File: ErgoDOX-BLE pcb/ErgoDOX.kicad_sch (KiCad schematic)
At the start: 113 parts, among them J1 Conn_01x04, J2 Conn_01x02_Female, J4 Conn_01x02, J5 Conn_01x02, J6 6PIN, P1 USB_C_Plug_USB2.0, Q1 Q_NPN_BCE, SW0:10 SW0:3, SW0:11 SW0:2, SW0:12 SW0:1, SW0:7 SW0:6, SW0:8 SW0:5, SW0:9 SW0:4, SW1:10 SW1:3, SW1:11 SW1:2, SW1:12 SW1:1, SW1:13 SW1:0, SW1:9 SW1:4, SW2:10 SW2:3, SW2:11 SW2:2, SW2:12 SW2:1, SW2:13 SW2:0, SW2:7 SW2:6, SW2:8 SW2:5, SW2:9 SW2:4, SW3:10 SW3:3, SW3:11 SW3:2, SW3:12 SW3:1, SW3:13 SW3:0, SW3:8 SW3:5, SW3:9 SW3:4, SW4:10 SW4:3, SW4:11 SW4:2, SW4:12 SW4:1, SW4:13 SW4:0, SW4:7 SW4:6, SW4:8 SW4:5, SW4:9 SW4:4, SW5:10 SW5:3, SW5:11 SW5:2, SW5:12 SW5:1, SW5:13 SW5:0, SW5:7 SW5:6, SW5:8 SW5:5, SW5:9 SW5:4, U1 MCP23018, U2 MCP73831-2-OT, U3 SPX3819M5-L-3-3

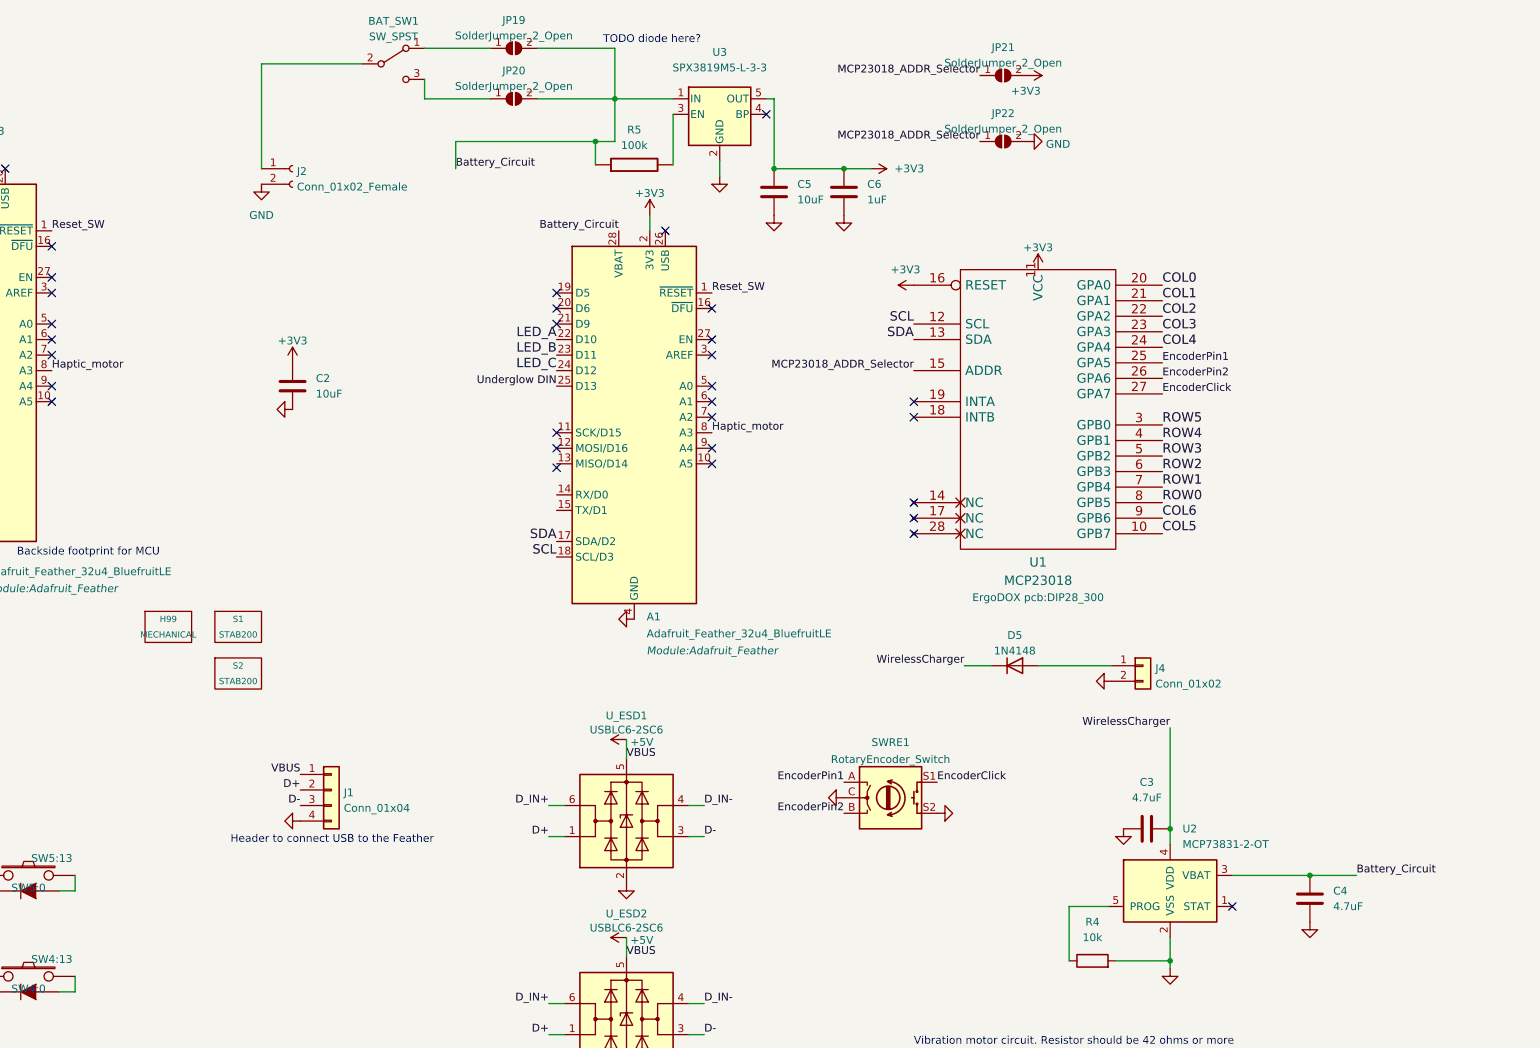
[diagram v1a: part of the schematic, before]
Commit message: Routing my days away
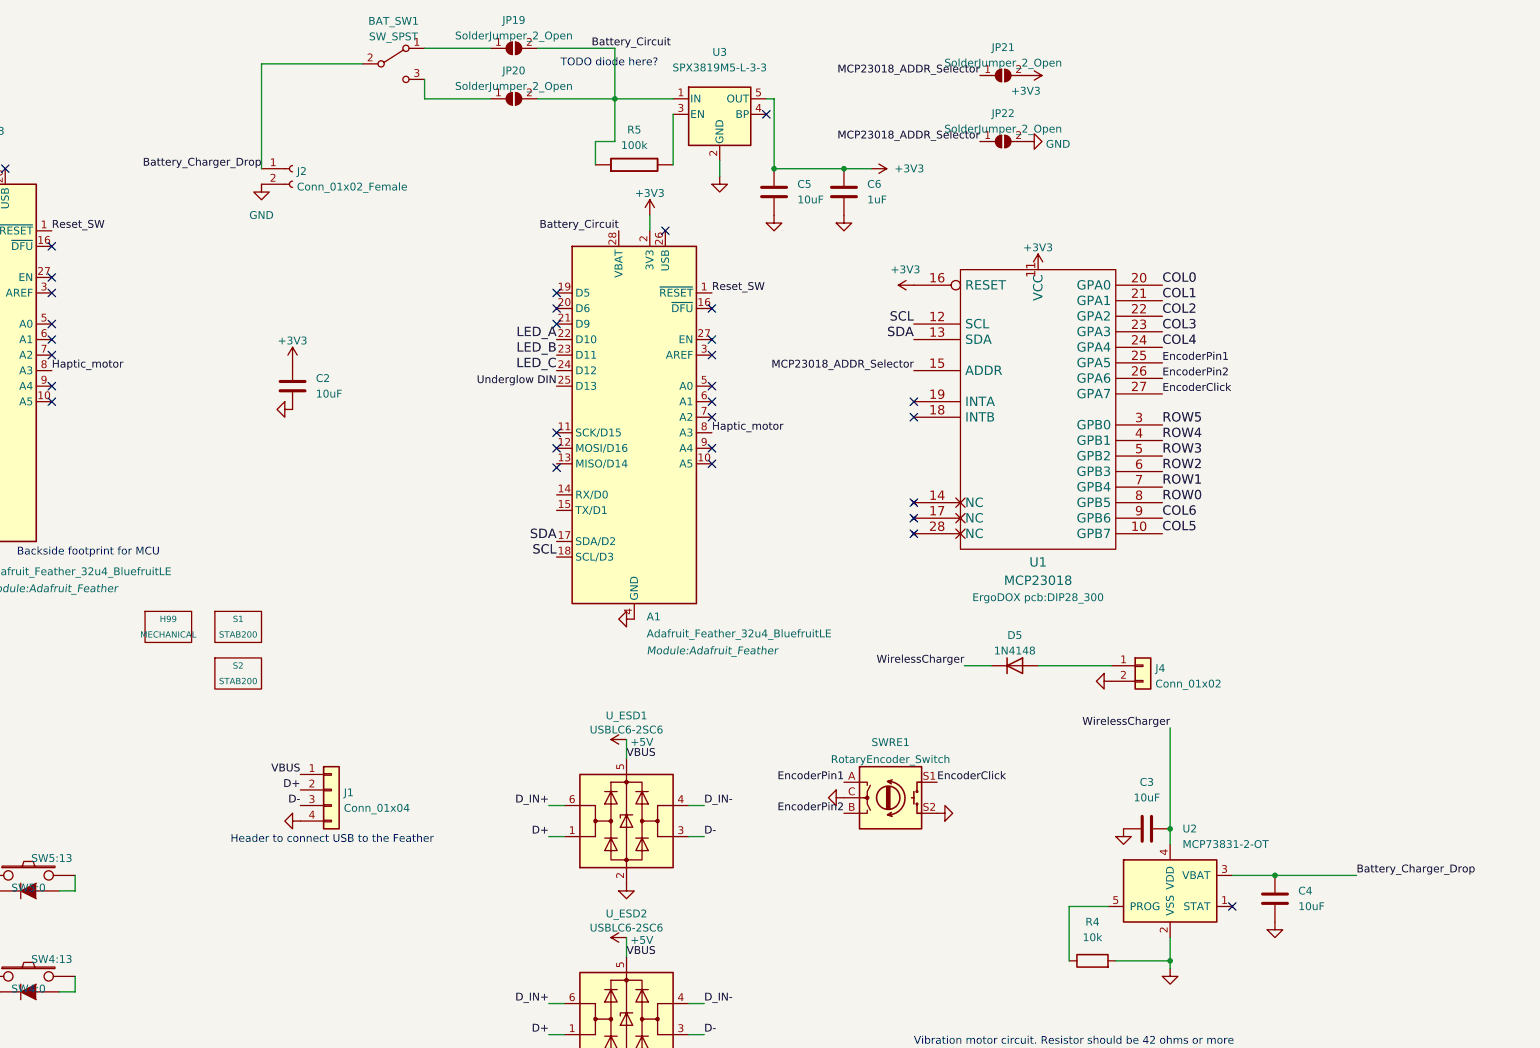
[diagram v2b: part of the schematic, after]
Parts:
- C3, C4: value 4.7uF -> 10uF; footprint (none) -> Capacitor_SMD:C_0805_2012Metric_Pad1.18x1.45mm_HandSolder; manf# (none) -> CC0805ZKY5V6BB106
- R4: footprint (none) -> Resistor_THT:R_Axial_DIN0207_L6.3mm_D2.5mm_P10.16mm_Horizontal
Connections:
- net Battery_Circuit: no longer C4.1, U2.3 (VBAT)
- net Battery_Charger_Drop: now reaches BAT_SW1.2 (B), J2.1 (Pin_1)
- net Battery_Charger_Drop: now also C4.1, U2.3 (VBAT)
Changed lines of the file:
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@@
   (junction (at 43.18 223.52) (diameter 0) (color 0 0 0 0)
   )
-  (junction (at 247.65 33.655) (diameter 0) (color 0 0 0 0)
-  )
   (junction (at 58.42 229.87) (diameter 0) (color 0 0 0 0)
   )
@@
   (junction (at 184.15 223.52) (diameter 0) (color 0 0 0 0)
   )
-  (junction (at 341.63 146.05) (diameter 0) (color 0 0 0 0)
+  (junction (at 358.775 153.67) (diameter 0) (color 0 0 0 0)
   )
   (junction (at 78.74 172.72) (diameter 0) (color 0 0 0 0)
@@
   (junction (at 111.76 229.87) (diameter 0) (color 0 0 0 0)
   )
-  (junction (at 364.49 153.67) (diameter 0) (color 0 0 0 0)
-  )
   (junction (at 93.98 213.36) (diameter 0) (color 0 0 0 0)
   )
+  (junction (at 341.63 146.05) (diameter 0) (color 0 0 0 0)
+  )
   (junction (at 149.86 222.25) (diameter 0) (color 0 0 0 0)
   )
@@
     (stroke (width 0) (type default) (color 0 0 0 0))
   )
-  (wire (pts (xy 224.79 33.655) (xy 247.65 33.655))
-    (stroke (width 0) (type default) (color 0 0 0 0))
-  )
   (wire (pts (xy 43.18 238.76) (xy 43.18 250.19))
     (stroke (width 0) (type default) (color 0 0 0 0))
   )
-  (wire (pts (xy 341.63 146.05) (xy 341.63 148.59))
+  (wire (pts (xy 341.63 129.54) (xy 341.63 146.05))
     (stroke (width 0) (type default) (color 0 0 0 0))
   )
@@
     (stroke (width 0) (type default) (color 0 0 0 0))
   )
-  (wire (pts (xy 364.49 153.67) (xy 372.11 153.67))
+  (wire (pts (xy 358.775 153.67) (xy 372.11 153.67))
     (stroke (width 0) (type default) (color 0 0 0 0))
   )
@@
     (stroke (width 0) (type default) (color 0 0 0 0))
   )
-  (wire (pts (xy 351.79 153.67) (xy 364.49 153.67))
+  (wire (pts (xy 351.79 153.67) (xy 358.775 153.67))
     (stroke (width 0) (type default) (color 0 0 0 0))
   )
@@
     (stroke (width 0) (type default) (color 0 0 0 0))
   )
-  (wire (pts (xy 341.63 129.54) (xy 341.63 146.05))
-    (stroke (width 0) (type default) (color 0 0 0 0))
-  )
   (wire (pts (xy 58.42 180.34) (xy 76.2 180.34))
     (stroke (width 0) (type default) (color 0 0 0 0))
@@
     (stroke (width 0) (type default) (color 0 0 0 0))
   )
-  (wire (pts (xy 224.79 33.655) (xy 224.79 38.1))
-    (stroke (width 0) (type default) (color 0 0 0 0))
-  )
   (wire (pts (xy 147.32 213.36) (xy 147.32 219.71))
     (stroke (width 0) (type default) (color 0 0 0 0))
@@
     (stroke (width 0) (type default) (color 0 0 0 0))
   )
+  (wire (pts (xy 341.63 146.05) (xy 341.63 148.59))
+    (stroke (width 0) (type default) (color 0 0 0 0))
+  )
   (wire (pts (xy 129.54 213.36) (xy 129.54 219.71))
     (stroke (width 0) (type default) (color 0 0 0 0))
@@
     (effects (font (size 1.27 1.27)) (justify left bottom))
   )
-  (text "TODO diode here?" (at 248.92 17.78 0)
+  (text "TODO diode here?" (at 241.935 21.59 0)
     (effects (font (size 1.27 1.27)) (justify left bottom))
   )
@@
     (effects (font (size 1.27 1.27)) (justify right bottom))
   )
-  (label "Battery_Circuit" (at 224.79 38.1 0)
-    (effects (font (size 1.27 1.27)) (justify left bottom))
-  )
   (label "D_IN_RIGHT-" (at 97.79 126.365 180)
     (effects (font (size 1.27 1.27)) (justify right bottom))
@@
     (effects (font (size 1.524 1.524)) (justify left bottom))
   )
+  (label "Battery_Charger_Drop" (at 193.04 38.1 180)
+    (effects (font (size 1.27 1.27)) (justify right bottom))
+  )
   (label "SCL" (at 241.3 101.6 180)
     (effects (font (size 1.524 1.524)) (justify right bottom))
@@
     (effects (font (size 1.27 1.27)) (justify left bottom))
   )
-  (label "Battery_Circuit" (at 372.11 153.67 0)
+  (label "Battery_Charger_Drop" (at 372.11 153.67 0)
     (effects (font (size 1.27 1.27)) (justify left bottom))
   )
@@
     (effects (font (size 1.27 1.27)) (justify left bottom))
   )
+  (label "Battery_Circuit" (at 247.015 18.415 0)
+    (effects (font (size 1.27 1.27)) (justify left bottom))
+  )
   (label "COL0" (at 149.86 250.19 270)
     (effects (font (size 1.524 1.524)) (justify right bottom))
@@
     (property "Reference" "R4" (id 0) (at 328.93 161.29 90))
     (property "Value" "10k" (id 1) (at 328.93 163.83 90))
-    (property "Footprint" "" (id 2) (at 328.93 169.418 90)
+    (property "Footprint" "Resistor_THT:R_Axial_DIN0207_L6.3mm_D2.5mm_P10.16mm_Horizontal" (id 2) (at 328.93 169.418 90)
       (effects (font (size 1.27 1.27)) hide)
     )
@@
     (pin "6")
   )
+  (symbol (lib_id "Device:C") (at 337.82 146.05 270) (unit 1)
+    (in_bom yes) (on_board yes) (fields_autoplaced)
+    (property "Reference" "C3" (id 0) (at 337.82 138.43 90))
+    (property "Value" "10uF" (id 1) (at 337.82 140.97 90))
+    (property "Footprint" "Capacitor_SMD:C_0805_2012Metric_Pad1.18x1.45mm_HandSolder" (id 2) (at 334.01 147.0152 0)
+      (effects (font (size 1.27 1.27)) hide)
+    )
+    (property "Datasheet" "https://www.yageo.com/upload/media/product/productsearch/datasheet/mlcc/UPY-GPHC_Y5V_6.3V-to-50V_11.pdf" (id 3) (at 337.82 146.05 0)
+      (effects (font (size 1.27 1.27)) hide)
+    )
+    (property "manf#" "CC0805ZKY5V6BB106" (id 4) (at 337.82 146.05 0)
+      (effects (font (size 1.27 1.27)) hide)
+    )
+    (pin "1")
+    (pin "2")
+  )
   (symbol (lib_id "Connector_Generic:Conn_01x02") (at 337.185 119.38 0) (unit 1)
     (in_bom yes) (on_board yes) (fields_autoplaced)
@@
     (pin "1")
   )
-  (symbol (lib_id "Device:C") (at 337.82 146.05 270) (unit 1)
-    (in_bom yes) (on_board yes) (fields_autoplaced)
-    (property "Reference" "C3" (id 0) (at 337.82 138.43 90))
-    (property "Value" "4.7uF" (id 1) (at 337.82 140.97 90))
-    (property "Footprint" "" (id 2) (at 334.01 147.0152 0)
-      (effects (font (size 1.27 1.27)) hide)
-    )
-    (property "Datasheet" "~" (id 3) (at 337.82 146.05 0)
-      (effects (font (size 1.27 1.27)) hide)
-    )
-    (pin "1")
-    (pin "2")
-  )
   (symbol (lib_name "SolderJumper_2_Open_1") (lib_id "Jumper:SolderJumper_2_Open") (at 307.975 237.49 0) (unit 1)
     (in_bom yes) (on_board yes)
@@
     (pin "2")
   )
-  (symbol (lib_id "component:GND") (at 364.49 162.56 0) (unit 1)
+  (symbol (lib_id "component:GND") (at 358.775 162.56 0) (unit 1)
     (in_bom yes) (on_board yes)
-    (property "Reference" "#PWR040" (id 0) (at 364.49 162.56 0)
+    (property "Reference" "#PWR040" (id 0) (at 358.775 162.56 0)
       (effects (font (size 0.762 0.762)) hide)
     )
-    (property "Value" "GND" (id 1) (at 364.49 164.338 0)
+    (property "Value" "GND" (id 1) (at 358.775 164.338 0)
       (effects (font (size 0.762 0.762)) hide)
     )
-    (property "Footprint" "" (id 2) (at 364.49 162.56 0)
+    (property "Footprint" "" (id 2) (at 358.775 162.56 0)
       (effects (font (size 1.27 1.27)) hide)
     )
-    (property "Datasheet" "" (id 3) (at 364.49 162.56 0)
+    (property "Datasheet" "" (id 3) (at 358.775 162.56 0)
       (effects (font (size 1.27 1.27)) hide)
     )
@@
     (pin "1")
   )
-  (symbol (lib_id "Device:C") (at 364.49 157.48 0) (unit 1)
-    (in_bom yes) (on_board yes) (fields_autoplaced)
-    (property "Reference" "C4" (id 0) (at 368.3 156.2099 0)
-      (effects (font (size 1.27 1.27)) (justify left))
-    )
-    (property "Value" "4.7uF" (id 1) (at 368.3 158.7499 0)
-      (effects (font (size 1.27 1.27)) (justify left))
-    )
-    (property "Footprint" "" (id 2) (at 365.4552 161.29 0)
-      (effects (font (size 1.27 1.27)) hide)
-    )
-    (property "Datasheet" "~" (id 3) (at 364.49 157.48 0)
-      (effects (font (size 1.27 1.27)) hide)
-    )
-    (pin "1")
-    (pin "2")
-  )
   (symbol (lib_id "Device:C") (at 288.29 41.91 0) (unit 1)
     (in_bom yes) (on_board yes) (fields_autoplaced)
@@
     (pin "2")
   )
+  (symbol (lib_id "Device:C") (at 358.775 157.48 0) (unit 1)
+    (in_bom yes) (on_board yes) (fields_autoplaced)
+    (property "Reference" "C4" (id 0) (at 362.585 156.2099 0)
+      (effects (font (size 1.27 1.27)) (justify left))
+    )
+    (property "Value" "10uF" (id 1) (at 362.585 158.7499 0)
+      (effects (font (size 1.27 1.27)) (justify left))
+    )
+    (property "Footprint" "Capacitor_SMD:C_0805_2012Metric_Pad1.18x1.45mm_HandSolder" (id 2) (at 359.7402 161.29 0)
+      (effects (font (size 1.27 1.27)) hide)
+    )
+    (property "Datasheet" "https://www.yageo.com/upload/media/product/productsearch/datasheet/mlcc/UPY-GPHC_Y5V_6.3V-to-50V_11.pdf" (id 3) (at 358.775 157.48 0)
+      (effects (font (size 1.27 1.27)) hide)
+    )
+    (property "manf#" "CC0805ZKY5V6BB106" (id 4) (at 358.775 157.48 0)
+      (effects (font (size 1.27 1.27)) hide)
+    )
+    (pin "1")
+    (pin "2")
+  )
   (symbol (lib_id "Switch:SW_SPDT") (at 214.63 20.955 0) (unit 1)
     (in_bom yes) (on_board yes)
@@
       (reference "C2") (unit 1) (value "10uF") (footprint "Capacitor_THT:C_Disc_D3.8mm_W2.6mm_P2.50mm")
     )
-    (path "/87c1b609-a25d-4f1a-b078-b9738040c2d4"
-      (reference "C3") (unit 1) (value "4.7uF") (footprint "")
+    (path "/5573bfb7-1fbc-4713-8b3e-20d1545510fe"
+      (reference "C3") (unit 1) (value "10uF") (footprint "Capacitor_SMD:C_0805_2012Metric_Pad1.18x1.45mm_HandSolder")
     )
-    (path "/cae143bf-2636-4103-a2b9-0d53b46d1a39"
-      (reference "C4") (unit 1) (value "4.7uF") (footprint "")
+    (path "/f7b52f61-c56e-4364-bc16-99bf9f5d71b0"
+      (reference "C4") (unit 1) (value "10uF") (footprint "Capacitor_SMD:C_0805_2012Metric_Pad1.18x1.45mm_HandSolder")
     )
     (path "/d186e3cc-ae10-40d5-a0ba-8749430f37fb"
@@
     )
     (path "/36a30954-1052-4da6-a55e-b0c8f21bcb14"
-      (reference "R4") (unit 1) (value "10k") (footprint "")
+      (reference "R4") (unit 1) (value "10k") (footprint "Resistor_THT:R_Axial_DIN0207_L6.3mm_D2.5mm_P10.16mm_Horizontal")
     )
     (path "/2261c62b-c1d7-43d6-829c-7da9168a6716"

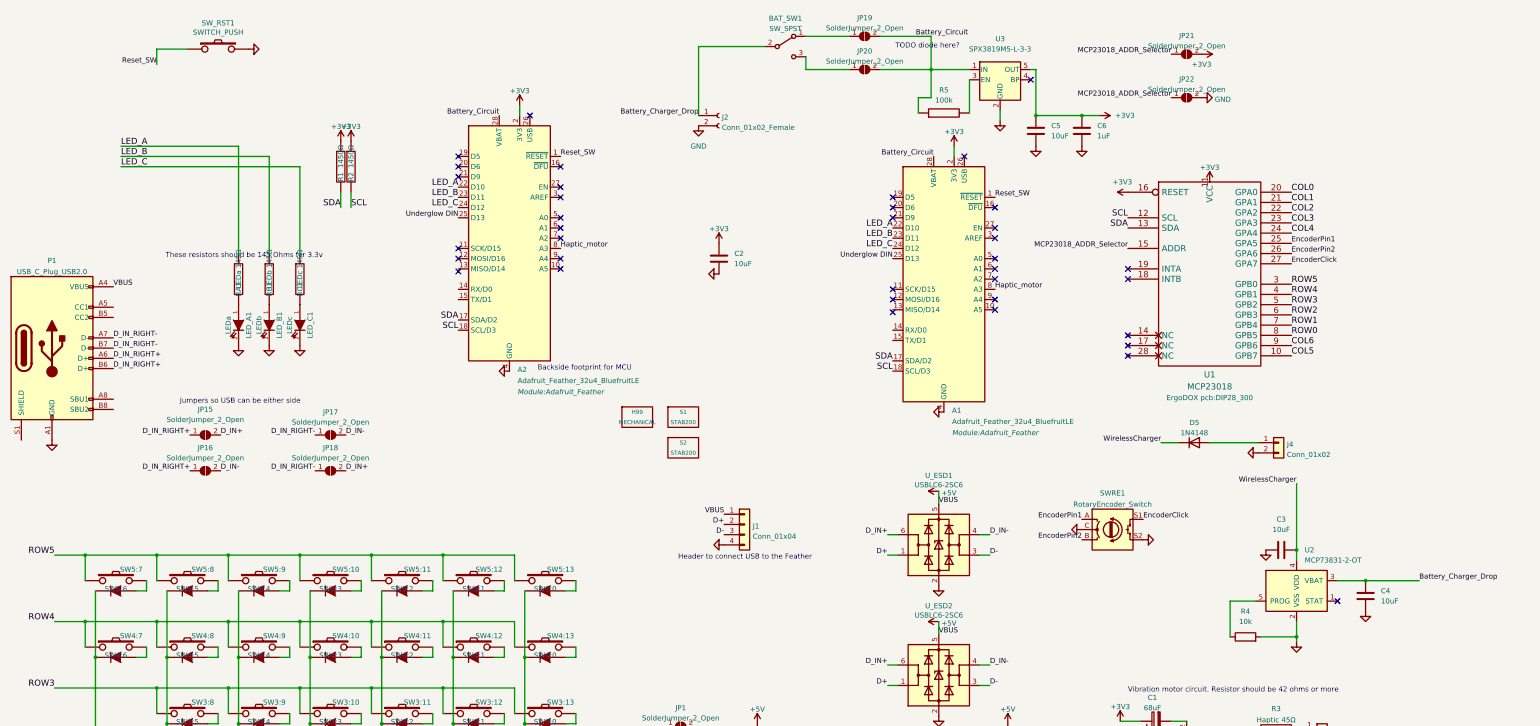
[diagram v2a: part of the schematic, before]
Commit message: Moving a bunch of stuff to SMD
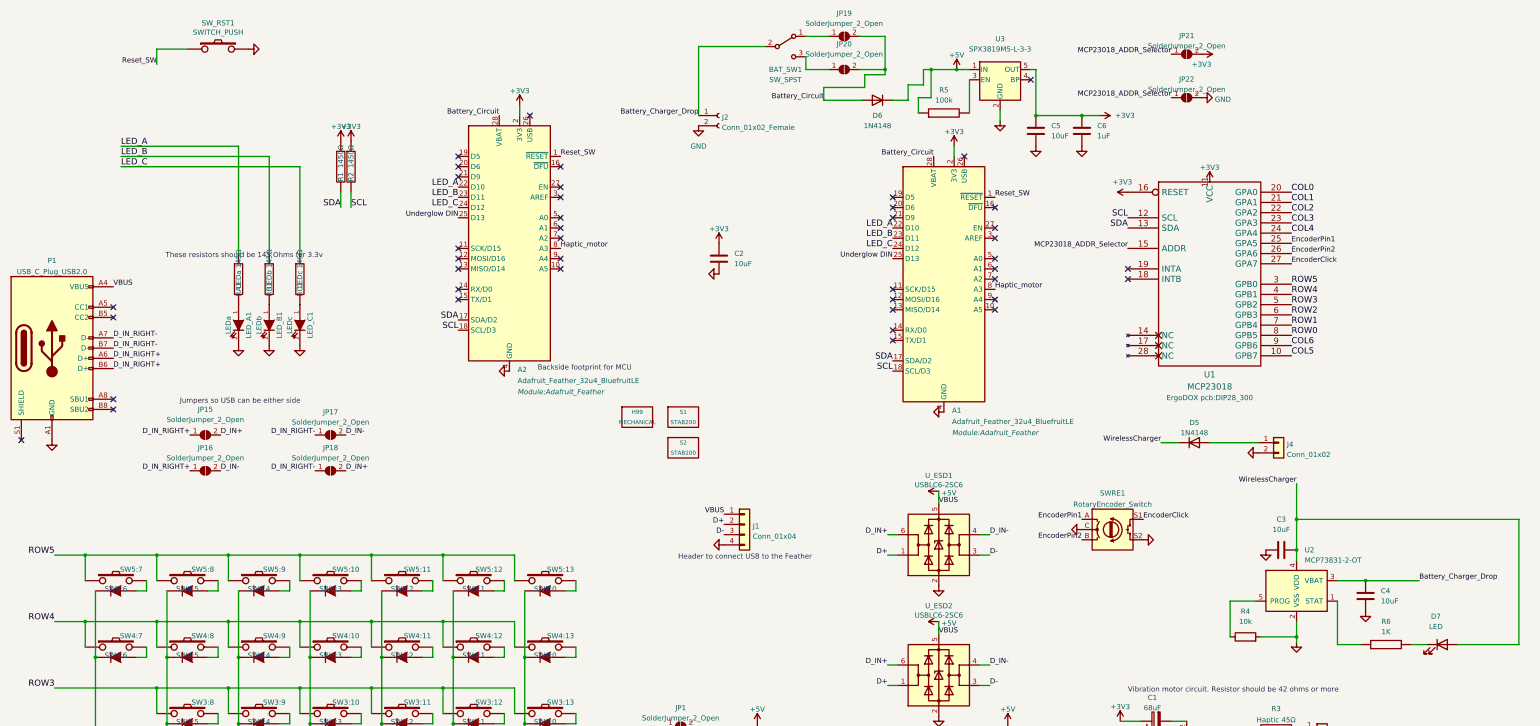
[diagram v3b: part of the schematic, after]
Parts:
- added D6: 1N4148, Diode_SMD:D_SOD-123, symbol Diode:1N4148
- added D7: LED, LED_SMD:LED_PLCC-2, symbol Device:LED
- added R6: 1K, Resistor_SMD:R_1206_3216Metric_Pad1.30x1.75mm_HandSolder, symbol component:RESISTOR
- R4: footprint Resistor_THT:R_Axial_DIN0207_L6.3mm_D2.5mm_P10.16mm_Horizontal -> Resistor_SMD:R_0805_2012Metric_Pad1.20x1.40mm_HandSolder; manf# (none) -> RC0805JR-0710KL
- R5: footprint Resistor_THT:R_Axial_DIN0207_L6.3mm_D2.5mm_P10.16mm_Horizontal -> Resistor_SMD:R_0603_1608Metric_Pad0.98x0.95mm_HandSolder; manf# CF18JT100K -> RNCF0603DTE100K
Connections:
- net +5V: now also R5.1, U3.1 (IN), D6.1 (K)
- net Battery_Circuit: now also D6.2 (A); no longer R5.1, U3.1 (IN)
- net WirelessCharger: now also D7.2 (A)
- net at U2.1 (STAT): now also R6.1
- new net: D7.1 (K), R6.2
- no-connect marks 39 -> 44
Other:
- note removed: "TODO diode here?"
- moved on the sheet: JP19, JP20
